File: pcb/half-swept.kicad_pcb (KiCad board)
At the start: 2 copper layers, 108.6 x 88.8 mm, 61 parts, among them J1 AudioJack4dpb, J2 AudioJack4dpb, SW1 SW_Push, SW10 SW_Push, SW11 SW_Push, SW12 SW_Push, SW14 SW_Push, SW15 SW_Push, SW16 SW_Push, SW17 SW_Push, SW18 SW_Push, SW2 SW_Push, SW20 SW_Push, SW21 SW_Push, SW3 SW_Push, SW4 SW_Push, SW5 SW_Push, SW6 SW_Push, SW8 SW_Push, SW9 SW_Push, U2 Elite-C

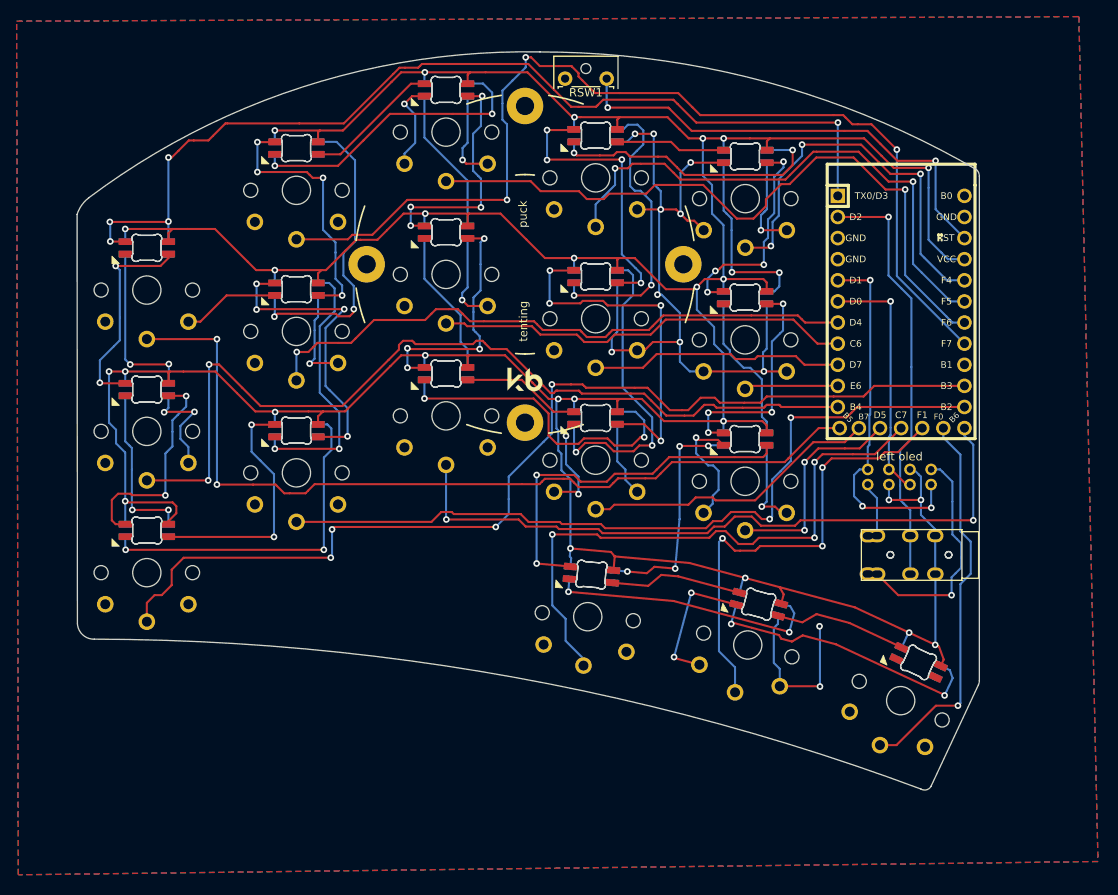
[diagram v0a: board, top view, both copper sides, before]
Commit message: added gateron ks-27 support on the same footprint, so now supports both choc v1 and ks-27
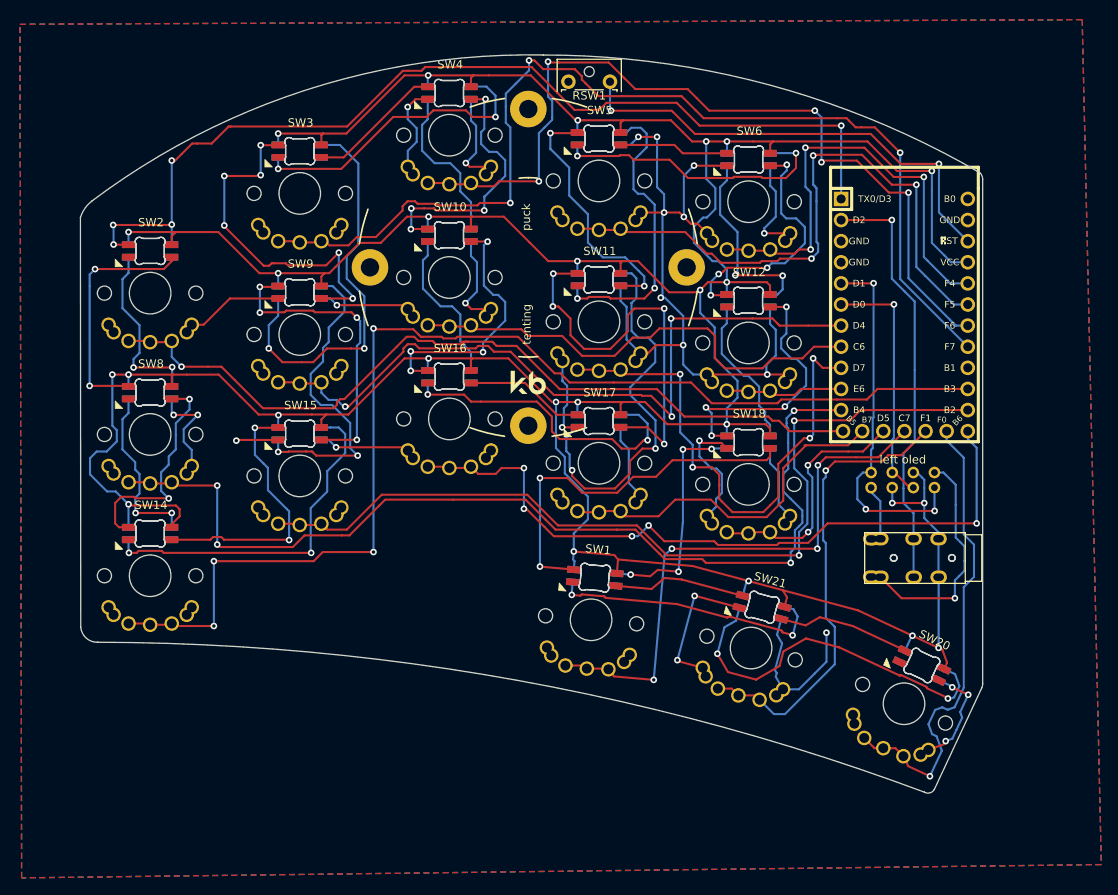
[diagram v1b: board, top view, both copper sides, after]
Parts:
- SW1, SW10, SW11, SW12, SW14, SW15, SW16, SW17, SW18, SW2, SW20, SW21, SW3, SW4, SW5, SW6, SW8, SW9: footprint Keebio-Parts:Kailh-PG1350-1u-reversible -> fingerpunch:gateron-ks27-choc-v1-reversible
- moved J1 0.55 mm to (120.5, 73.1)
- moved D10 0.55 mm to (40.4, 63.2)
- moved D28 0.55 mm to (40.4, 63.2)
- moved SW15 0.55 mm to (40.4, 63.2)
- moved D18 0.55 mm to (113.1, 90.6)
- moved D36 0.55 mm to (113.1, 90.6)
- moved SW20 0.55 mm to (113.1, 90.6)
- moved D14 0.55 mm to (76.4, 44.7)
- moved D32 0.55 mm to (76.4, 44.7)
- moved SW11 0.55 mm to (76.4, 44.7)
- moved OL1 0.55 mm to (113.0, 62.8)
- moved D13 0.55 mm to (40.4, 46.2)
- moved D31 0.55 mm to (40.4, 46.2)
- moved SW9 0.55 mm to (40.4, 46.2)
- moved D27 0.55 mm to (94.4, 64.2)
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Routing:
- net Switch9: track 30.6 -> 62.2 mm, vias 0 -> 4
- net gnd: track 294.4 -> 314.9 mm, vias 25 -> 26
- net Switch3: track 83.4 -> 102.2 mm, vias 1 -> 5
- net Switch11: track 123.6 -> 141.0 mm
- net Switch7: track 73.5 -> 89.3 mm, vias 1 -> 3
- net Switch12: track 94.1 -> 106.5 mm
- net Net-(D13-Pad2): track 37.3 -> 48.4 mm
- net Switch6: track 107.9 -> 118.9 mm, vias 2 -> 4
- net Net-(D31-Pad2): track 31.9 -> 42.8 mm, vias 4 -> 6
- net Switch16: track 46.7 -> 56.7 mm
- net Net-(D15-Pad2): track 34.9 -> 44.8 mm
- net vcc: track 485.5 -> 494.9 mm
- net Switch4: track 65.7 -> 75.1 mm, vias 2 -> 3
- net Net-(D11-Pad2): track 38.4 -> 47.6 mm
- net Switch14: track 36.0 -> 43.1 mm
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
